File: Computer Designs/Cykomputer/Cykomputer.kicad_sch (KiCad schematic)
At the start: 76 parts, among them J1 Bus_ISA_8bit, J10 DE15_Socket_HighDensity_Mount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, J11 USB_C_Receptacle, J12 IEC_60320_C14_Receptacle, J13 Conn_01x02, J14 PINHD_1x2_Male, J15 Bus_ISA_8bit, J16 Conn_02x12_Row_Letter_First, J17 Conn_01x12, J18 AudioJack2, J19 Conn_01x32, J2 Bus_ISA_8bit, J20 Conn_01x09, J3 Bus_ISA_8bit, J4 DE9_Pins_MountingHoles, J5 DE9_Pins_MountingHoles, J6 Mini-DIN-6, J7 DE15_Socket_HighDensity_Mount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, J8 DE15_Socket_HighDensity_Mount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, J9 DE15_Socket_HighDensity_Mount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, SW1 SW_SPST, SW2 SW_Rotary_1x7_MP, SW3 Push_Button, U1 W65C02SxP, U10 74HC14, U11 W65C51NxP, U12 W65C02SxP, U13 27C256, U14 KM62256CLP, U15 KM62256CLP, U16 27C256, U17 74HCT595, U18 74HCT164, U19 KM62256CLP, U20 4053, U21 MIC2025-2YM, U22 W65C22SxP, U23 74HCT595, U24 74HCT595, U25 KM62256CLP, U26 W65C22SxP, U27 CH340G, U28 DS1813-5, U29 CH376S, U30 6581, U4 W65C22SxP, U5 W65C51NxP, U6 W65C51NxP, U7 MAX232, U8 MAX232, U9 W65C22SxP, Y1 ACO-xxxMHz-A, Y2 ACO-xxxMHz-A, Y3 ACO-xxxMHz-A, Y4 ACO-xxxMHz-A, Y5 ACO-xxxMHz-A, Y6 ACO-xxxMHz-A, Y7 ACO-xxxMHz-A

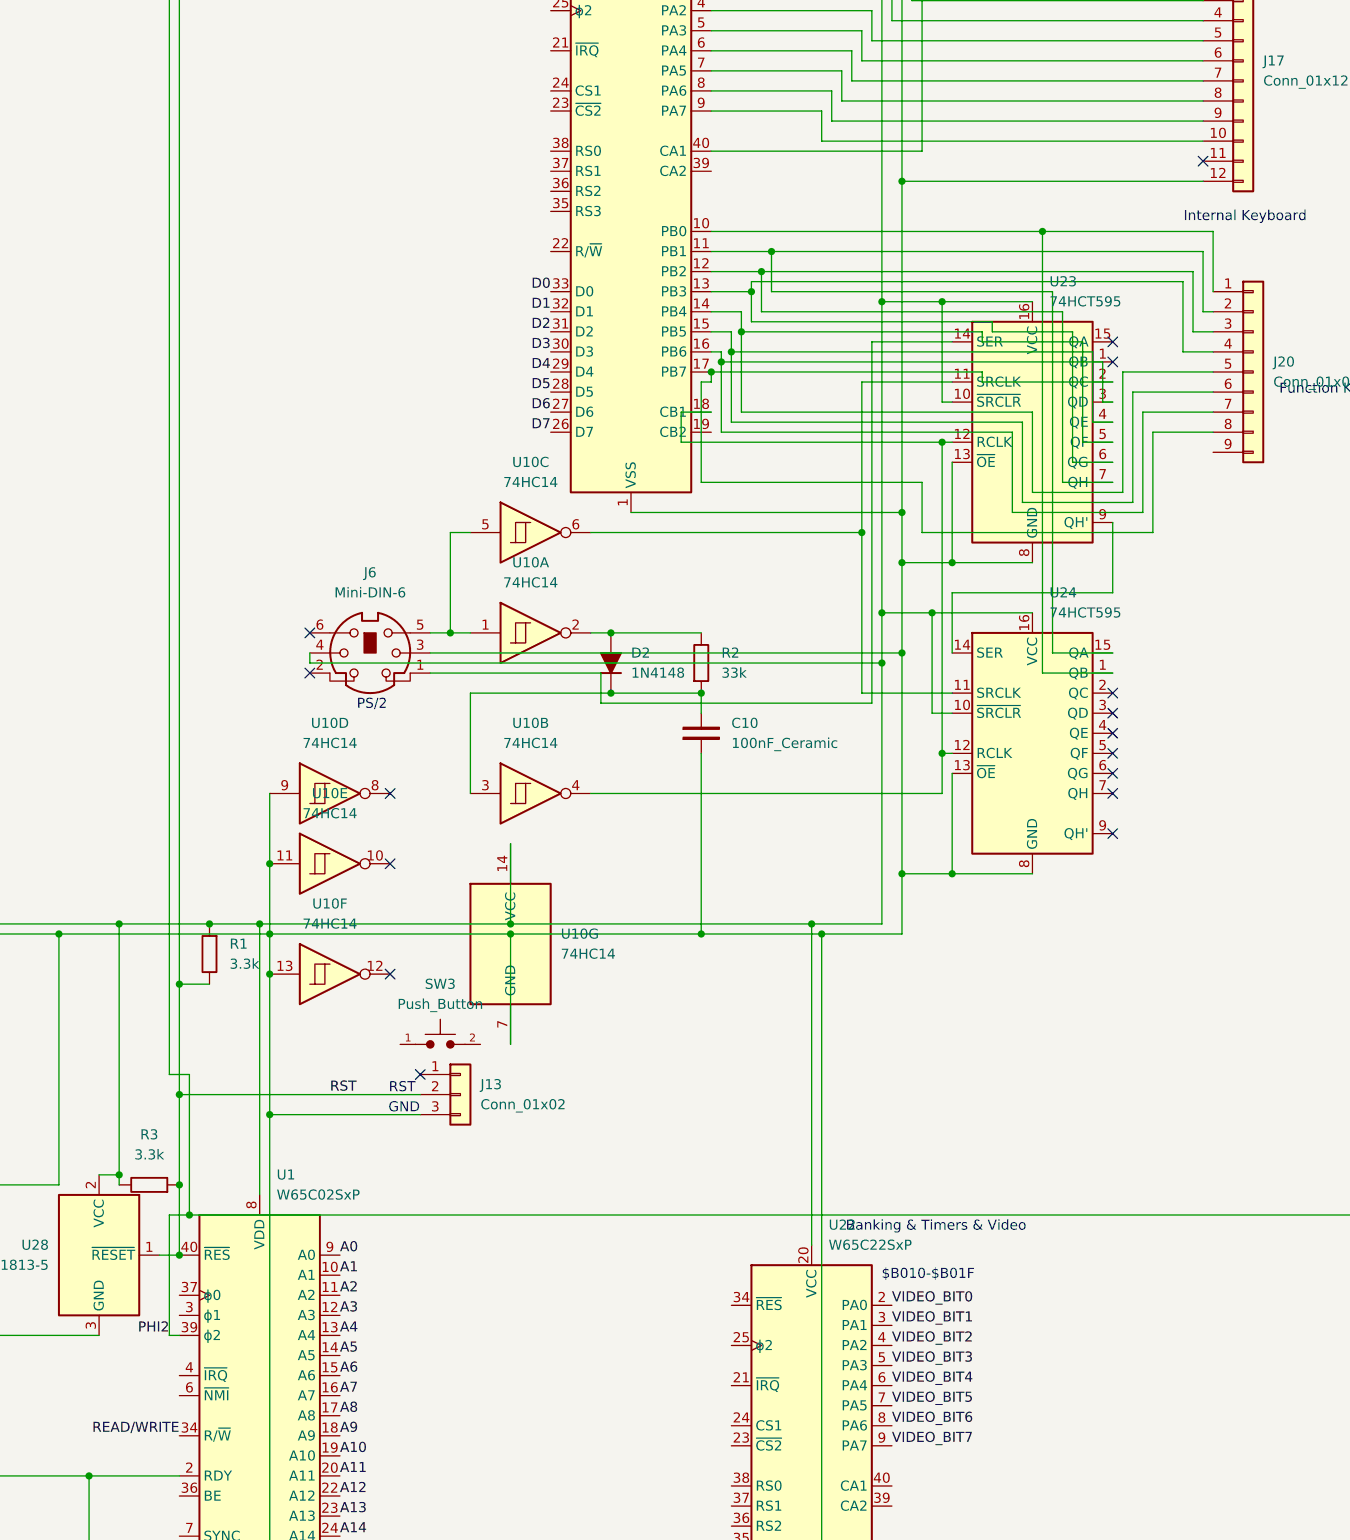
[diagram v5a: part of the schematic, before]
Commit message: Added Wozmon file and test.cfg, continued kernel
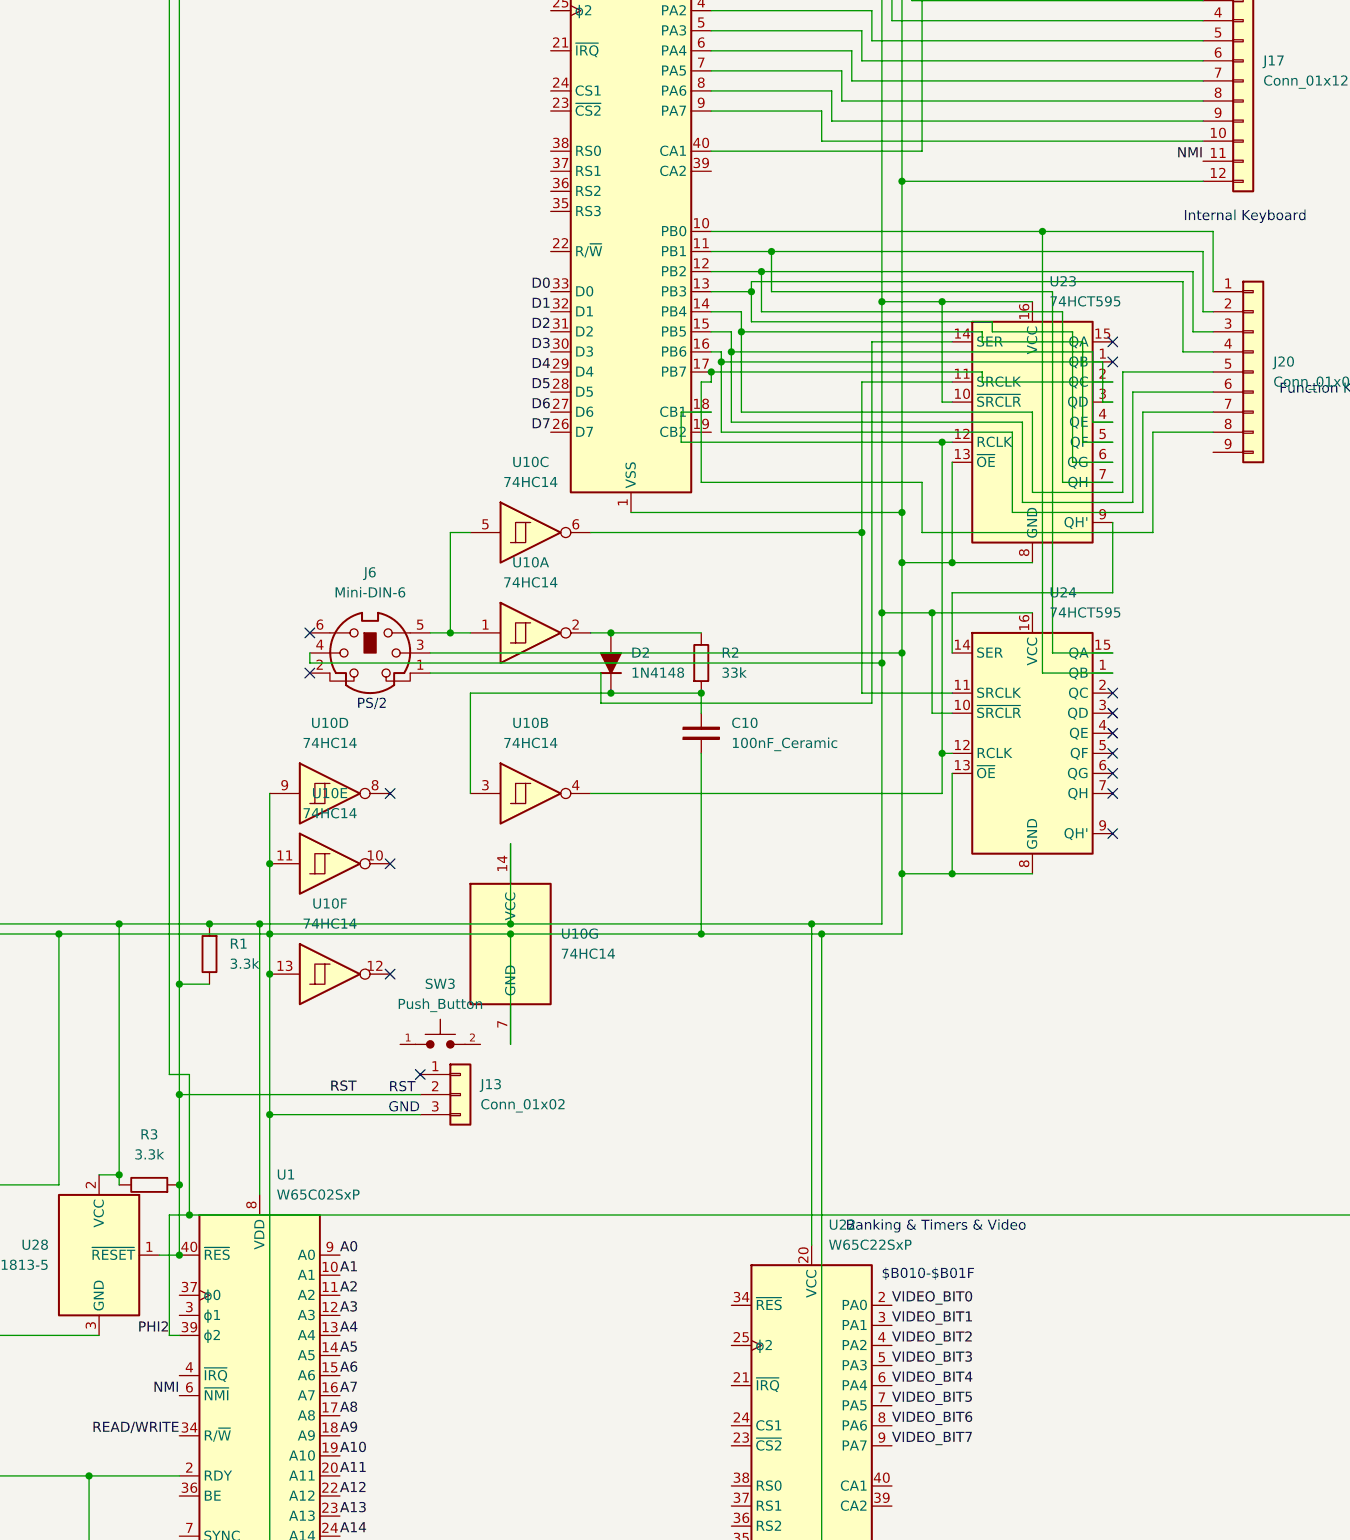
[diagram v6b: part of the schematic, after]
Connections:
- net NMI: now reaches J17.11 (Pin_11)
- net NMI: now also U1.6 (~{NMI})
- no-connect marks 45 -> 44
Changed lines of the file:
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@@
 	)
 	(no_connect
-		(at 490.22 251.46)
-	)
-	(no_connect
 		(at 613.41 325.12)
 	)
@@
 		)
 	)
+	(label "NMI"
+		(at 360.68 407.67 180)
+		(effects
+			(font
+				(size 1.27 1.27)
+			)
+			(justify right bottom)
+		)
+	)
+	(label "NMI"
+		(at 490.22 251.46 180)
+		(effects
+			(font
+				(size 1.27 1.27)
+			)
+			(justify right bottom)
+		)
+	)

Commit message: Continued
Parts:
- added U2: 74LS30, symbol 74xx:74LS30
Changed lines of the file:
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@@
+	)
+	(symbol
+		(lib_id "74xx:74LS30")
+		(at 175.26 490.22 270)
+		(unit 2)
+		(body_style 1)
+		(exclude_from_sim no)
+		(in_bom yes)
+		(on_board yes)
+		(in_pos_files yes)
+		(dnp no)
+		(fields_autoplaced yes)
+		(property "Reference" "U2"
+			(at 175.26 480.06 90)
+			(show_name no)
+			(do_not_autoplace no)
+			(effects
+				(font
+					(size 1.27 1.27)
+				)
+			)
+		)
+		(property "Value" "74LS30"
+			(at 175.26 482.6 90)
+			(show_name no)
+			(do_not_autoplace no)
+			(effects
+				(font
+					(size 1.27 1.27)
+				)
+			)
+		)
+		(property "Footprint" ""
+			(at 175.26 490.22 0)
+			(hide yes)
+			(show_name no)
+			(do_not_autoplace no)
+			(effects
+				(font
+					(size 1.27 1.27)
+				)
+			)
+		)
+		(property "Datasheet" "http://www.ti.com/lit/gpn/sn74LS30"
+			(at 175.26 490.22 0)
+			(hide yes)
+			(show_name no)
+			(do_not_autoplace no)
+			(effects
+				(font
+					(size 1.27 1.27)
+				)
+			)
+		)
+		(property "Description" "8-input NAND"
+			(at 175.26 490.22 0)
+			(hide yes)
+			(show_name no)
+			(do_not_autoplace no)
+			(effects
+				(font
+					(size 1.27 1.27)
+				)
+			)
+		)
+		(pin "12"
+		)
+		(pin "11"
+		)
+		(pin "1"
+		)
+		(pin "2"
+		)
+		(pin "3"
+		)
+		(pin "5"
+		)
+		(pin "4"
+		)
+		(pin "8"
+		)
+		(pin "6"
+		)
+		(pin "7"
+		)
+		(pin "14"
+		)
+		(instances
+			(project "Cykomputer"
+				(path "/7319cfd4-b54a-49cd-84bf-92265ba5acc0"
+					(reference "U2")
+					(unit 2)
+				)
+			)
+		)
 	)
 	(symbol
@@
 				)
 			)
+		)
+	)
+	(symbol
+		(lib_id "74xx:74LS30")
+		(at 262.89 334.01 180)
+		(unit 1)
+		(body_style 1)
+		(exclude_from_sim no)
+		(in_bom yes)
+		(on_board yes)
+		(in_pos_files yes)
+		(dnp no)
+		(fields_autoplaced yes)
+		(property "Reference" "U2"
+			(at 262.8983 318.77 0)
+			(show_name no)
+			(do_not_autoplace no)
+			(effects
+				(font
+					(size 1.27 1.27)
+				)
+			)
+		)
+		(property "Value" "74LS30"
+			(at 262.8983 321.31 0)
+			(show_name no)
+			(do_not_autoplace no)
+			(effects
+				(font
+					(size 1.27 1.27)
+				)
+			)
+		)
+		(property "Footprint" ""
+			(at 262.89 334.01 0)
+			(hide yes)
+			(show_name no)
+			(do_not_autoplace no)
+			(effects
+				(font
+					(size 1.27 1.27)
+				)
+			)
+		)
+		(property "Datasheet" "http://www.ti.com/lit/gpn/sn74LS30"
+			(at 262.89 334.01 0)
+			(hide yes)
+			(show_name no)
+			(do_not_autoplace no)
+			(effects
+				(font
+					(size 1.27 1.27)
+				)
+			)
+		)
+		(property "Description" "8-input NAND"
+			(at 262.89 334.01 0)
+			(hide yes)
+			(show_name no)
+			(do_not_autoplace no)
+			(effects
+				(font
+					(size 1.27 1.27)
+				)
+			)
+		)
+		(pin "12"
+		)
+		(pin "11"
+		)
+		(pin "1"
+		)
+		(pin "2"
+		)
+		(pin "3"
+		)
+		(pin "5"
+		)
+		(pin "4"
+		)
+		(pin "8"
+		)
+		(pin "6"
+		)
+		(pin "7"
+		)
+		(pin "14"
+		)
+		(instances
+			(project "Cykomputer"
+				(path "/7319cfd4-b54a-49cd-84bf-92265ba5acc0"
+					(reference "U2")
+					(unit 1)
+				)
+			)

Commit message: Finished Keyboard Design
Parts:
- removed U27: CH340G, Package_SO:SOIC-16_3.9x9.9mm_P1.27mm, symbol Interface_USB:CH340G
- added R4, R6: 5.1k, PCM_4ms_Resistor:R_Axial_DIN0207_L6.3mm_D2.5mm_P7.62mm_Horizontal, symbol PCM_SparkFun-Resistor:5.1k_0603
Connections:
- net GND: now also R4.1, R6.1
- net at J11.A5 (CC1): now also R6.2
- net at J11.A6 (D+), J11.B6 (D+): now also U29.10 (UD+)
- net at J11.A7 (D-), J11.B7 (D-): now also U29.11 (UD-)
- net at J11.B5 (CC2): now also R4.2
